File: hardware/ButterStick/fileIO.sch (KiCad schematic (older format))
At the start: 6 parts, among them J1 SYZYGY-STD, J10 SYZYGY-STD, J2 JST GH Series, J8 SYZYGY-STD

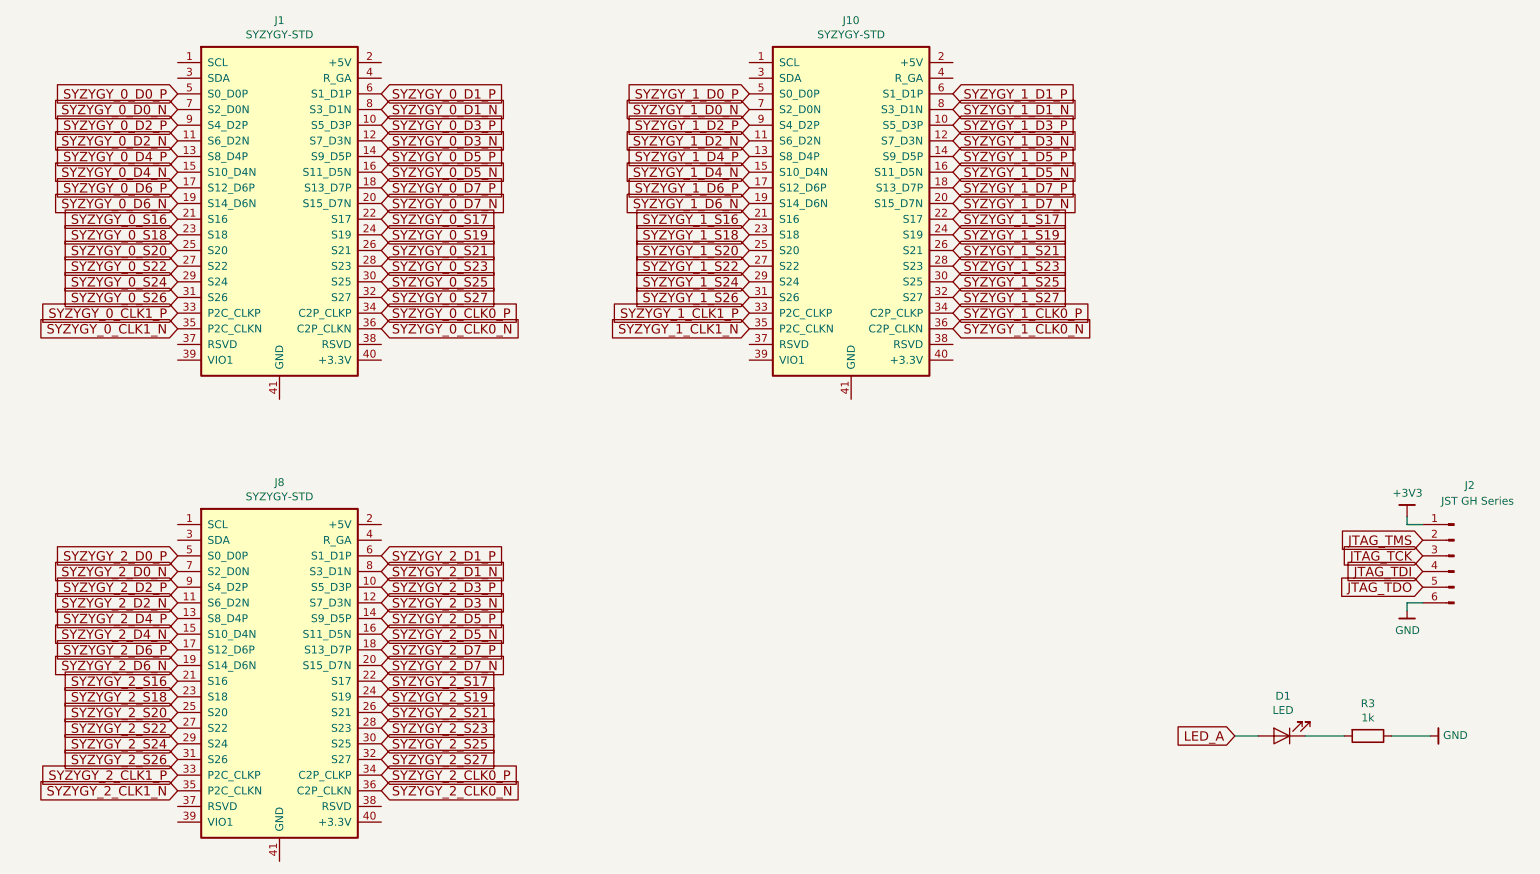
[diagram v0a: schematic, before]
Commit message: Update schematic hieracy layout.
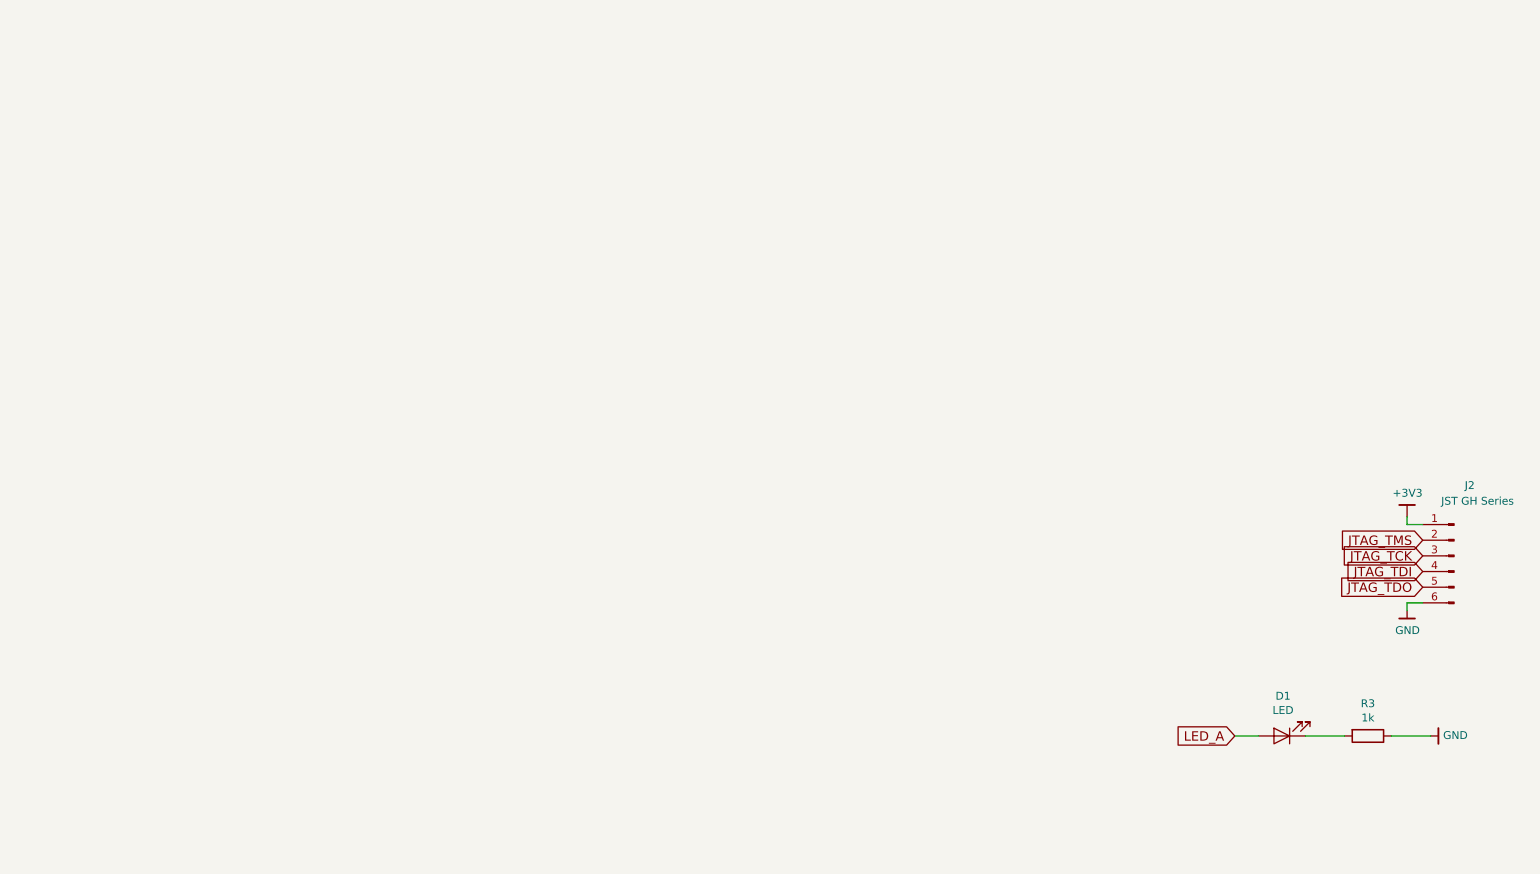
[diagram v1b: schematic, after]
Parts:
- removed J1, J10, J8: SYZYGY-STD, symbol gkl_misc:SYZYGY-STD
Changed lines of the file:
@@
 $Descr A4 11693 8268
 encoding utf-8
-Sheet 5 7
+Sheet 5 13
 Title ""
 Date ""
@@
 Wire Wire Line
 	9500 4950 9500 5000
-$Comp
-L gkl_misc:SYZYGY-STD J8
-U 1 1 5CACDB71
-P 2300 5300
-F 0 "J8" H 2300 6419 50  0000 C CNN
-F 1 "SYZYGY-STD" H 2300 6328 50  0000 C CNN
-F 2 "" H 2300 6300 50  0001 C CNN
-F 3 "" H 2300 6300 50  0001 C CNN
-	1    2300 5300
-	1    0    0    -1
-$EndComp
-$Comp
-L gkl_misc:SYZYGY-STD J1
-U 1 1 5CACDBDB
-P 2300 2350
-F 0 "J1" H 2300 3469 50  0000 C CNN
-F 1 "SYZYGY-STD" H 2300 3378 50  0000 C CNN
-F 2 "" H 2300 3350 50  0001 C CNN
-F 3 "" H 2300 3350 50  0001 C CNN
-	1    2300 2350
-	1    0    0    -1
-$EndComp
-$Comp
-L gkl_misc:SYZYGY-STD J10
-U 1 1 5CACDC45
-P 5950 2350
-F 0 "J10" H 5950 3469 50  0000 C CNN
-F 1 "SYZYGY-STD" H 5950 3378 50  0000 C CNN
-F 2 "" H 5950 3350 50  0001 C CNN
-F 3 "" H 5950 3350 50  0001 C CNN
-	1    5950 2350
-	1    0    0    -1
-$EndComp
-Text GLabel 1650 1700 0    60   Input ~ 0
-SYZYGY_0_D0_P
-Text GLabel 1650 1800 0    60   Input ~ 0
-SYZYGY_0_D0_N
-Text GLabel 2950 1700 2    60   Input ~ 0
-SYZYGY_0_D1_P
-Text GLabel 2950 1800 2    60   Input ~ 0
-SYZYGY_0_D1_N
-Text GLabel 1650 1900 0    60   Input ~ 0
-SYZYGY_0_D2_P
-Text GLabel 1650 2000 0    60   Input ~ 0
-SYZYGY_0_D2_N
-Text GLabel 2950 1900 2    60   Input ~ 0
-SYZYGY_0_D3_P
-Text GLabel 2950 2000 2    60   Input ~ 0
-SYZYGY_0_D3_N
-Text GLabel 1650 2100 0    60   Input ~ 0
-SYZYGY_0_D4_P
-Text GLabel 1650 2200 0    60   Input ~ 0
-SYZYGY_0_D4_N
-Text GLabel 2950 2200 2    60   Input ~ 0
-SYZYGY_0_D5_N
-Text GLabel 2950 2100 2    60   Input ~ 0
-SYZYGY_0_D5_P
-Text GLabel 1650 2400 0    60   Input ~ 0
-SYZYGY_0_D6_N
-Text GLabel 1650 2300 0    60   Input ~ 0
-SYZYGY_0_D6_P
-Text GLabel 2950 3200 2    60   Input ~ 0
-SYZYGY_0_CLK0_N
-Text GLabel 2950 3100 2    60   Input ~ 0
-SYZYGY_0_CLK0_P
-Text GLabel 1650 3200 0    60   Input ~ 0
-SYZYGY_0_CLK1_N
-Text GLabel 1650 3100 0    60   Input ~ 0
-SYZYGY_0_CLK1_P
-Text GLabel 2950 2400 2    60   Input ~ 0
-SYZYGY_0_D7_N
-Text GLabel 2950 2300 2    60   Input ~ 0
-SYZYGY_0_D7_P
-Text GLabel 1650 2500 0    60   Input ~ 0
-SYZYGY_0_S16
-Text GLabel 2950 2500 2    60   Input ~ 0
-SYZYGY_0_S17
-Text GLabel 1650 2600 0    60   Input ~ 0
-SYZYGY_0_S18
-Text GLabel 2950 2600 2    60   Input ~ 0
-SYZYGY_0_S19
-Text GLabel 1650 2700 0    60   Input ~ 0
-SYZYGY_0_S20
-Text GLabel 2950 2700 2    60   Input ~ 0
-SYZYGY_0_S21
-Text GLabel 1650 2800 0    60   Input ~ 0
-SYZYGY_0_S22
-Text GLabel 2950 2800 2    60   Input ~ 0
-SYZYGY_0_S23
-Text GLabel 1650 2900 0    60   Input ~ 0
-SYZYGY_0_S24
-Text GLabel 2950 2900 2    60   Input ~ 0
-SYZYGY_0_S25
-Text GLabel 1650 3000 0    60   Input ~ 0
-SYZYGY_0_S26
-Text GLabel 2950 3000 2    60   Input ~ 0
-SYZYGY_0_S27
-Text GLabel 5300 1700 0    60   Input ~ 0
-SYZYGY_1_D0_P
-Text GLabel 5300 1800 0    60   Input ~ 0
-SYZYGY_1_D0_N
-Text GLabel 6600 1700 2    60   Input ~ 0
-SYZYGY_1_D1_P
-Text GLabel 6600 1800 2    60   Input ~ 0
-SYZYGY_1_D1_N
-Text GLabel 5300 1900 0    60   Input ~ 0
-SYZYGY_1_D2_P
-Text GLabel 5300 2000 0    60   Input ~ 0
-SYZYGY_1_D2_N
-Text GLabel 6600 1900 2    60   Input ~ 0
-SYZYGY_1_D3_P
-Text GLabel 6600 2000 2    60   Input ~ 0
-SYZYGY_1_D3_N
-Text GLabel 5300 2100 0    60   Input ~ 0
-SYZYGY_1_D4_P
-Text GLabel 5300 2200 0    60   Input ~ 0
-SYZYGY_1_D4_N
-Text GLabel 6600 2200 2    60   Input ~ 0
-SYZYGY_1_D5_N
-Text GLabel 6600 2100 2    60   Input ~ 0
-SYZYGY_1_D5_P
-Text GLabel 5300 2400 0    60   Input ~ 0
-SYZYGY_1_D6_N
-Text GLabel 5300 2300 0    60   Input ~ 0
-SYZYGY_1_D6_P
-Text GLabel 6600 3200 2    60   Input ~ 0
-SYZYGY_1_CLK0_N
-Text GLabel 6600 3100 2    60   Input ~ 0
-SYZYGY_1_CLK0_P
-Text GLabel 5300 3200 0    60   Input ~ 0
-SYZYGY_1_CLK1_N
-Text GLabel 5300 3100 0    60   Input ~ 0
-SYZYGY_1_CLK1_P
-Text GLabel 6600 2400 2    60   Input ~ 0
-SYZYGY_1_D7_N
-Text GLabel 6600 2300 2    60   Input ~ 0
-SYZYGY_1_D7_P
-Text GLabel 1650 4650 0    60   Input ~ 0
-SYZYGY_2_D0_P
-Text GLabel 1650 4750 0    60   Input ~ 0
-SYZYGY_2_D0_N
-Text GLabel 2950 4650 2    60   Input ~ 0
-SYZYGY_2_D1_P
-Text GLabel 2950 4750 2    60   Input ~ 0
-SYZYGY_2_D1_N
-Text GLabel 1650 4850 0    60   Input ~ 0
-SYZYGY_2_D2_P
-Text GLabel 1650 4950 0    60   Input ~ 0
-SYZYGY_2_D2_N
-Text GLabel 2950 4850 2    60   Input ~ 0
-SYZYGY_2_D3_P
-Text GLabel 2950 4950 2    60   Input ~ 0
-SYZYGY_2_D3_N
-Text GLabel 1650 5050 0    60   Input ~ 0
-SYZYGY_2_D4_P
-Text GLabel 1650 5150 0    60   Input ~ 0
-SYZYGY_2_D4_N
-Text GLabel 2950 5150 2    60   Input ~ 0
-SYZYGY_2_D5_N
-Text GLabel 2950 5050 2    60   Input ~ 0
-SYZYGY_2_D5_P
-Text GLabel 1650 5350 0    60   Input ~ 0
-SYZYGY_2_D6_N
-Text GLabel 1650 5250 0    60   Input ~ 0
-SYZYGY_2_D6_P
-Text GLabel 2950 6150 2    60   Input ~ 0
-SYZYGY_2_CLK0_N
-Text GLabel 2950 6050 2    60   Input ~ 0
-SYZYGY_2_CLK0_P
-Text GLabel 1650 6150 0    60   Input ~ 0
-SYZYGY_2_CLK1_N
-Text GLabel 1650 6050 0    60   Input ~ 0
-SYZYGY_2_CLK1_P
-Text GLabel 2950 5350 2    60   Input ~ 0
-SYZYGY_2_D7_N
-Text GLabel 2950 5250 2    60   Input ~ 0
-SYZYGY_2_D7_P
-Text GLabel 1650 5450 0    60   Input ~ 0
-SYZYGY_2_S16
-Text GLabel 2950 5450 2    60   Input ~ 0
-SYZYGY_2_S17
-Text GLabel 1650 5550 0    60   Input ~ 0
-SYZYGY_2_S18
-Text GLabel 2950 5550 2    60   Input ~ 0
-SYZYGY_2_S19
-Text GLabel 1650 5650 0    60   Input ~ 0
-SYZYGY_2_S20
-Text GLabel 2950 5650 2    60   Input ~ 0
-SYZYGY_2_S21
-Text GLabel 1650 5750 0    60   Input ~ 0
-SYZYGY_2_S22
-Text GLabel 2950 5750 2    60   Input ~ 0
-SYZYGY_2_S23
-Text GLabel 1650 5850 0    60   Input ~ 0
-SYZYGY_2_S24
-Text GLabel 2950 5850 2    60   Input ~ 0
-SYZYGY_2_S25
-Text GLabel 1650 5950 0    60   Input ~ 0
-SYZYGY_2_S26
-Text GLabel 2950 5950 2    60   Input ~ 0
-SYZYGY_2_S27
-Text GLabel 5300 2500 0    60   Input ~ 0
-SYZYGY_1_S16
-Text GLabel 6600 2500 2    60   Input ~ 0
-SYZYGY_1_S17
-Text GLabel 5300 2600 0    60   Input ~ 0
-SYZYGY_1_S18
-Text GLabel 6600 2600 2    60   Input ~ 0
-SYZYGY_1_S19
-Text GLabel 5300 2700 0    60   Input ~ 0
-SYZYGY_1_S20
-Text GLabel 6600 2700 2    60   Input ~ 0
-SYZYGY_1_S21
-Text GLabel 5300 2800 0    60   Input ~ 0
-SYZYGY_1_S22
-Text GLabel 6600 2800 2    60   Input ~ 0
-SYZYGY_1_S23
-Text GLabel 5300 2900 0    60   Input ~ 0
-SYZYGY_1_S24
-Text GLabel 6600 2900 2    60   Input ~ 0
-SYZYGY_1_S25
-Text GLabel 5300 3000 0    60   Input ~ 0
-SYZYGY_1_S26
-Text GLabel 6600 3000 2    60   Input ~ 0
-SYZYGY_1_S27
 $EndSCHEMATC

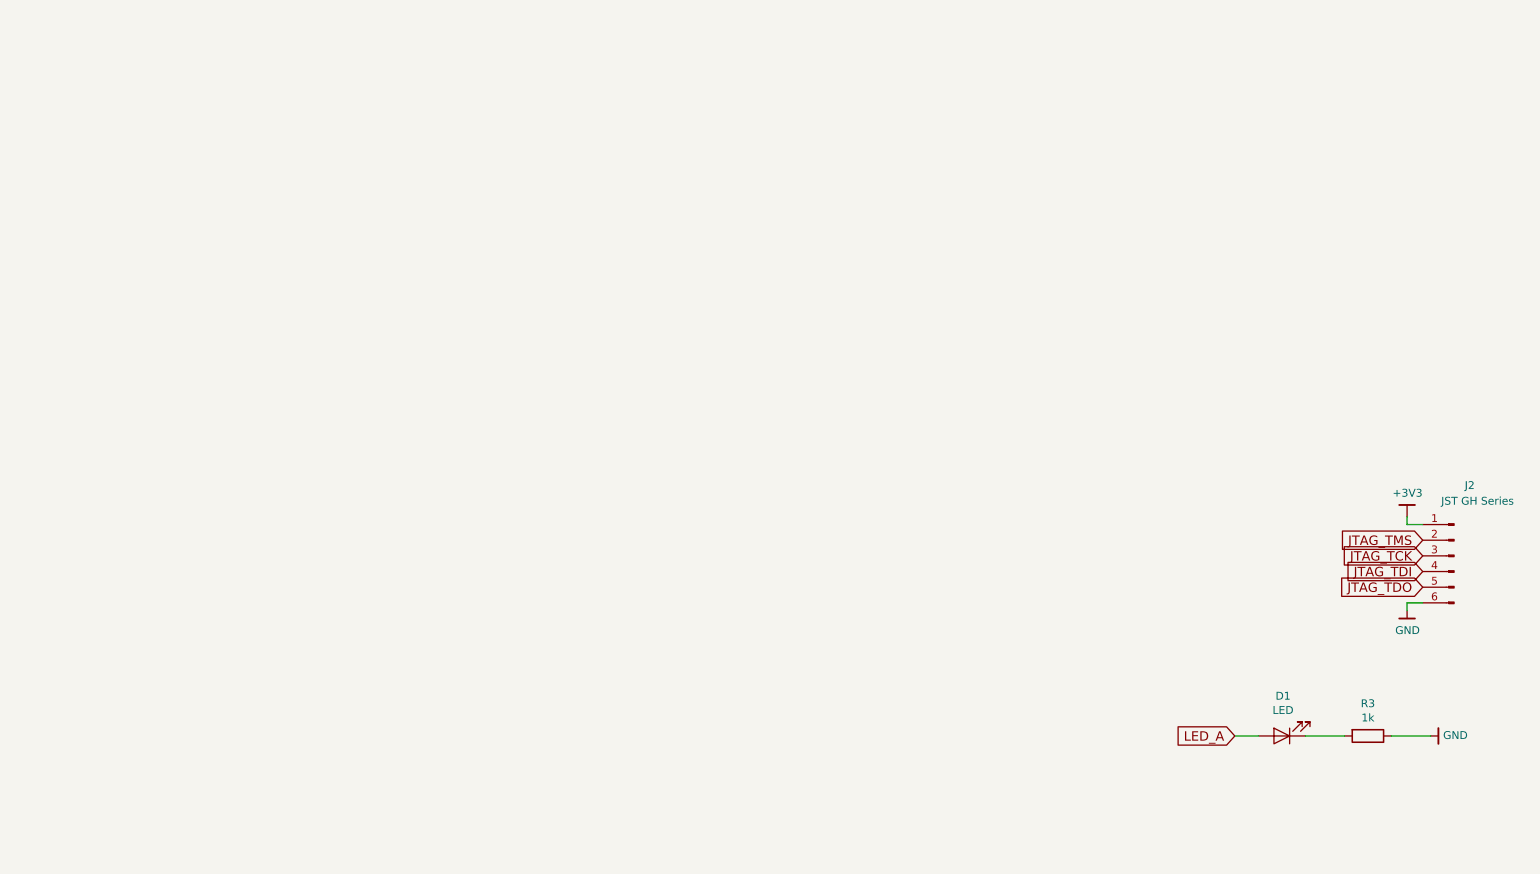
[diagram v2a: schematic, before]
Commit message: Added ESD on SD card signals.
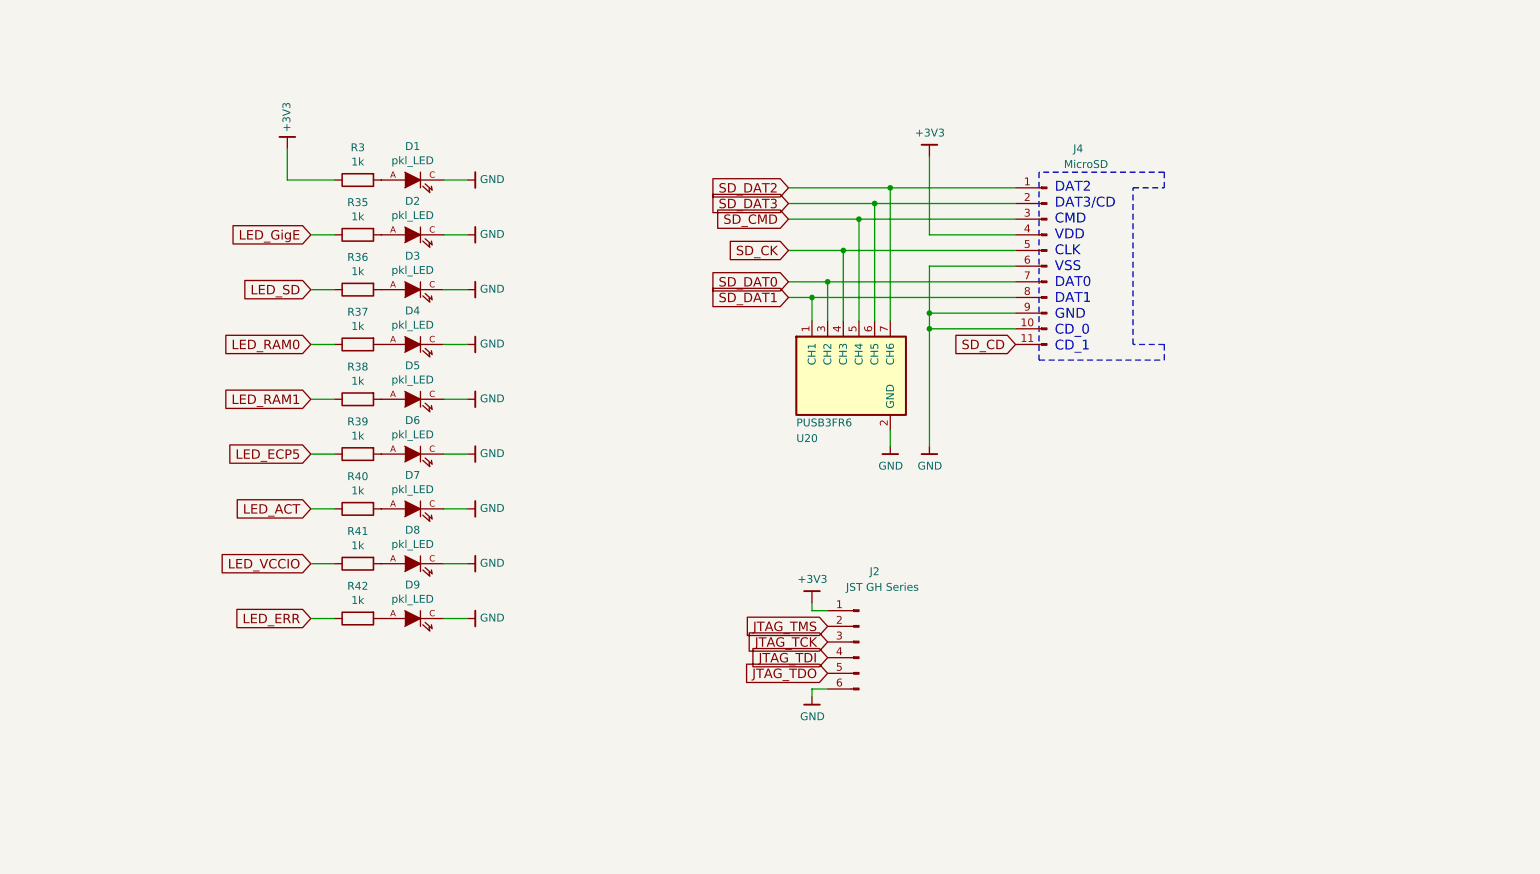
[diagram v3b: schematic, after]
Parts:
- removed D1: LED, LEDs:LED_0402, symbol Device:LED
- added D1, D2, D3, D4, D5, D6, D7, D8, D9: pkl_LED, pkl_dipol:D_0603, symbol pkl_device:pkl_LED
- added J4: MicroSD, gkl_conn:molex_microsd_1040310811, symbol Connector:Conn_01x11_Male
- added R35, R36, R37, R38, R39, R40, R41, R42: 1k, pkl_dipol:R_0402, symbol Device:R
- added U20: PUSB3FR6, gkl_housings_son:XSON7, symbol gkl_misc:PUSB3FR6
- R3: footprint Resistors_SMD:R_0402 -> pkl_dipol:R_0402
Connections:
- net +3V3: now also R3.1, J4.4 (Pin_4)
- net GND: now also D1.C, D2.C, D3.C, D4.C, D5.C, D6.C, D7.C, D8.C, D9.C, J4.10 (Pin_10), J4.6 (Pin_6), J4.9 (Pin_9), U20.2 (GND); no longer R3.1
- net at R3.2: now also D1.A
- new net: D2.A, R35.2
- new net: D3.A, R36.2
- new net: D4.A, R37.2
- new net: D5.A, R38.2
- new net: D6.A, R39.2
- new net: D7.A, R40.2
- new net: D8.A, R41.2
- new net: D9.A, R42.2
- new net LED_ACT: R40.1
- new net LED_ECP5: R39.1
- new net LED_ERR: R42.1
- new net LED_GigE: R35.1
- new net LED_RAM0: R37.1
- new net LED_RAM1: R38.1
- new net LED_SD: R36.1
- new net LED_VCCIO: R41.1
- new net SD_CD: J4.11 (Pin_11)
- new net SD_CK: J4.5 (Pin_5), U20.4 (CH3)
- new net SD_CMD: J4.3 (Pin_3), U20.5 (CH4)
- new net SD_DAT0: J4.7 (Pin_7), U20.3 (CH2)
- new net SD_DAT1: J4.8 (Pin_8), U20.1 (CH1)
- new net SD_DAT2: J4.1 (Pin_1), U20.7 (CH6)
- new net SD_DAT3: J4.2 (Pin_2), U20.6 (CH5)
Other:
- note added: "DAT2\nDAT3/CD\nCMD\nVDD\nCLK\nVSS\nDAT0\nDAT1\nGND\nCD_0\nCD_1\n"
- moved on the sheet: J2, R3

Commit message: Update KiCad PCB.
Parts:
- U20: MFG (none) -> Nexperia USA Inc.; PN (none) -> PUSB3FR6Z
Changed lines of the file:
@@
 F 2 "gkl_housings_son:XSON7" H 5950 3900 50  0001 C CNN
 F 3 "" H 5950 3900 50  0001 C CNN
+F 4 "Nexperia USA Inc." H 0   0   50  0001 C CNN "MFG"
+F 5 "PUSB3FR6Z" H 0   0   50  0001 C CNN "PN"
 	1    5950 3500
 	0    -1   1    0

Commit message: Finalised part values update BOM values to reflect. Swapped layers 4/5 due to stackup changes
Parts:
- D1, D2, D3, D4, D5, D6, D7, D8, D9: Mfg (none) -> Lite-On Inc.; PN (none) -> LTST-C190GKT
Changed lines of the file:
@@
 EESchema Schematic File Version 4
 LIBS:ButterStick-cache
-EELAYER 26 0
+EELAYER 29 0
 EELAYER END
 $Descr A4 11693 8268
 encoding utf-8
-Sheet 4 13
-Title ""
-Date ""
-Rev ""
-Comp ""
+Sheet 2 13
+Title "ButterStick"
+Date "2019-03-19"
+Rev "r0_1"
+Comp "GsD"
 Comment1 ""
 Comment2 ""
@@
 F 2 "pkl_dipol:D_0603" H 3150 2250 60  0001 C CNN
 F 3 "" H 3150 2250 60  0000 C CNN
+F 4 "Lite-On Inc." H 0   0   50  0001 C CNN "Mfg"
+F 5 "LTST-C190GKT" H 0   0   50  0001 C CNN "PN"
 	1    3150 2250
 	1    0    0    -1
@@
 F 2 "pkl_dipol:D_0603" H 3150 2600 60  0001 C CNN
 F 3 "" H 3150 2600 60  0000 C CNN
+F 4 "Lite-On Inc." H 0   0   50  0001 C CNN "Mfg"
+F 5 "LTST-C190GKT" H 0   0   50  0001 C CNN "PN"
 	1    3150 2600
 	1    0    0    -1
@@
 F 2 "pkl_dipol:D_0603" H 3150 2950 60  0001 C CNN
 F 3 "" H 3150 2950 60  0000 C CNN
+F 4 "Lite-On Inc." H 0   0   50  0001 C CNN "Mfg"
+F 5 "LTST-C190GKT" H 0   0   50  0001 C CNN "PN"
 	1    3150 2950
 	1    0    0    -1
@@
 F 2 "pkl_dipol:D_0603" H 3150 3300 60  0001 C CNN
 F 3 "" H 3150 3300 60  0000 C CNN
+F 4 "Lite-On Inc." H 0   0   50  0001 C CNN "Mfg"
+F 5 "LTST-C190GKT" H 0   0   50  0001 C CNN "PN"
 	1    3150 3300
 	1    0    0    -1
@@
 F 2 "pkl_dipol:D_0603" H 3150 3650 60  0001 C CNN
 F 3 "" H 3150 3650 60  0000 C CNN
+F 4 "Lite-On Inc." H 0   0   50  0001 C CNN "Mfg"
+F 5 "LTST-C190GKT" H 0   0   50  0001 C CNN "PN"
 	1    3150 3650
 	1    0    0    -1
@@
 F 2 "pkl_dipol:D_0603" H 3150 4000 60  0001 C CNN
 F 3 "" H 3150 4000 60  0000 C CNN
+F 4 "Lite-On Inc." H 0   0   50  0001 C CNN "Mfg"
+F 5 "LTST-C190GKT" H 0   0   50  0001 C CNN "PN"
 	1    3150 4000
 	1    0    0    -1
@@
 F 2 "pkl_dipol:D_0603" H 3150 4350 60  0001 C CNN
 F 3 "" H 3150 4350 60  0000 C CNN
+F 4 "Lite-On Inc." H 0   0   50  0001 C CNN "Mfg"
+F 5 "LTST-C190GKT" H 0   0   50  0001 C CNN "PN"
 	1    3150 4350
 	1    0    0    -1
@@
 F 2 "pkl_dipol:D_0603" H 3150 4700 60  0001 C CNN
 F 3 "" H 3150 4700 60  0000 C CNN
+F 4 "Lite-On Inc." H 0   0   50  0001 C CNN "Mfg"
+F 5 "LTST-C190GKT" H 0   0   50  0001 C CNN "PN"
 	1    3150 4700
 	1    0    0    -1
@@
 F 2 "pkl_dipol:D_0603" H 3150 5050 60  0001 C CNN
 F 3 "" H 3150 5050 60  0000 C CNN
+F 4 "Lite-On Inc." H 0   0   50  0001 C CNN "Mfg"
+F 5 "LTST-C190GKT" H 0   0   50  0001 C CNN "PN"
 	1    3150 5050
 	1    0    0    -1
